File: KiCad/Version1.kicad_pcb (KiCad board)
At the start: 2 copper layers, 41 x 77.7 mm, 82 parts, among them J1 SWD, J2 B4B-XH-A, J3 Conn_01x03_Male, SW1 SW_DPST_x2, SW2 RND 210-00662, SW8 Rotary_Encoder, U1 STM32F411RETx, U2 PMW3389, U3 USBLC6-2P6, U4 AP131-15, U5 AP1117-15, U6 Button, U7 Button, U8 Scroll_button, U9 Button, Y1 16Mhz

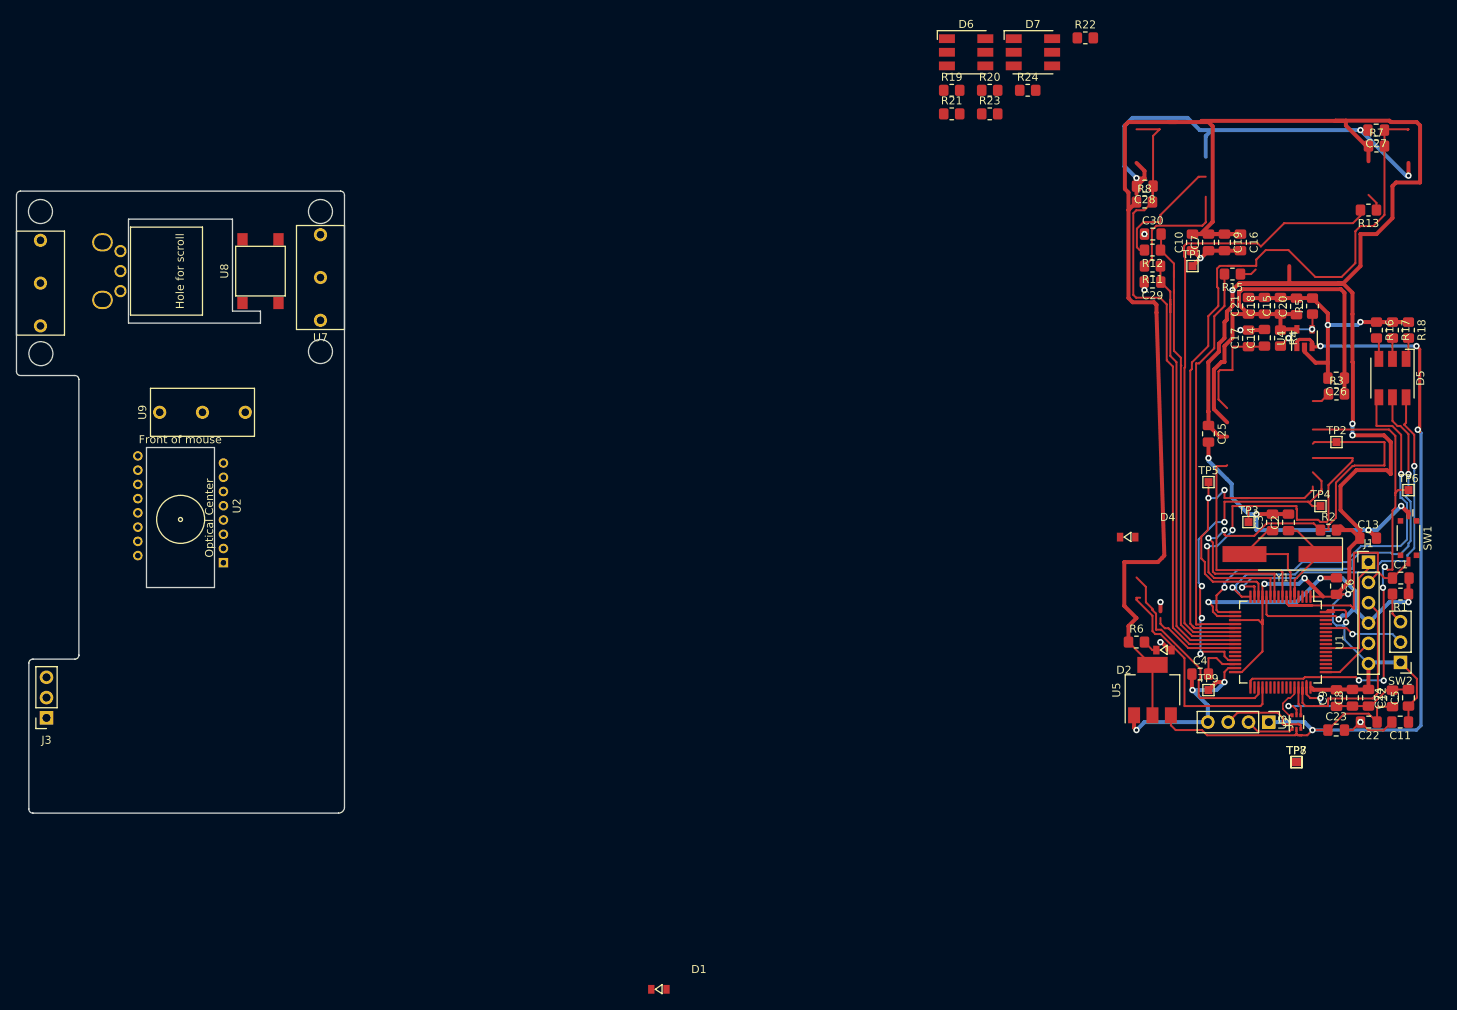
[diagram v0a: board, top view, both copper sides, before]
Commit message: Fixed almost all footprints and nearly the layout of the pcb
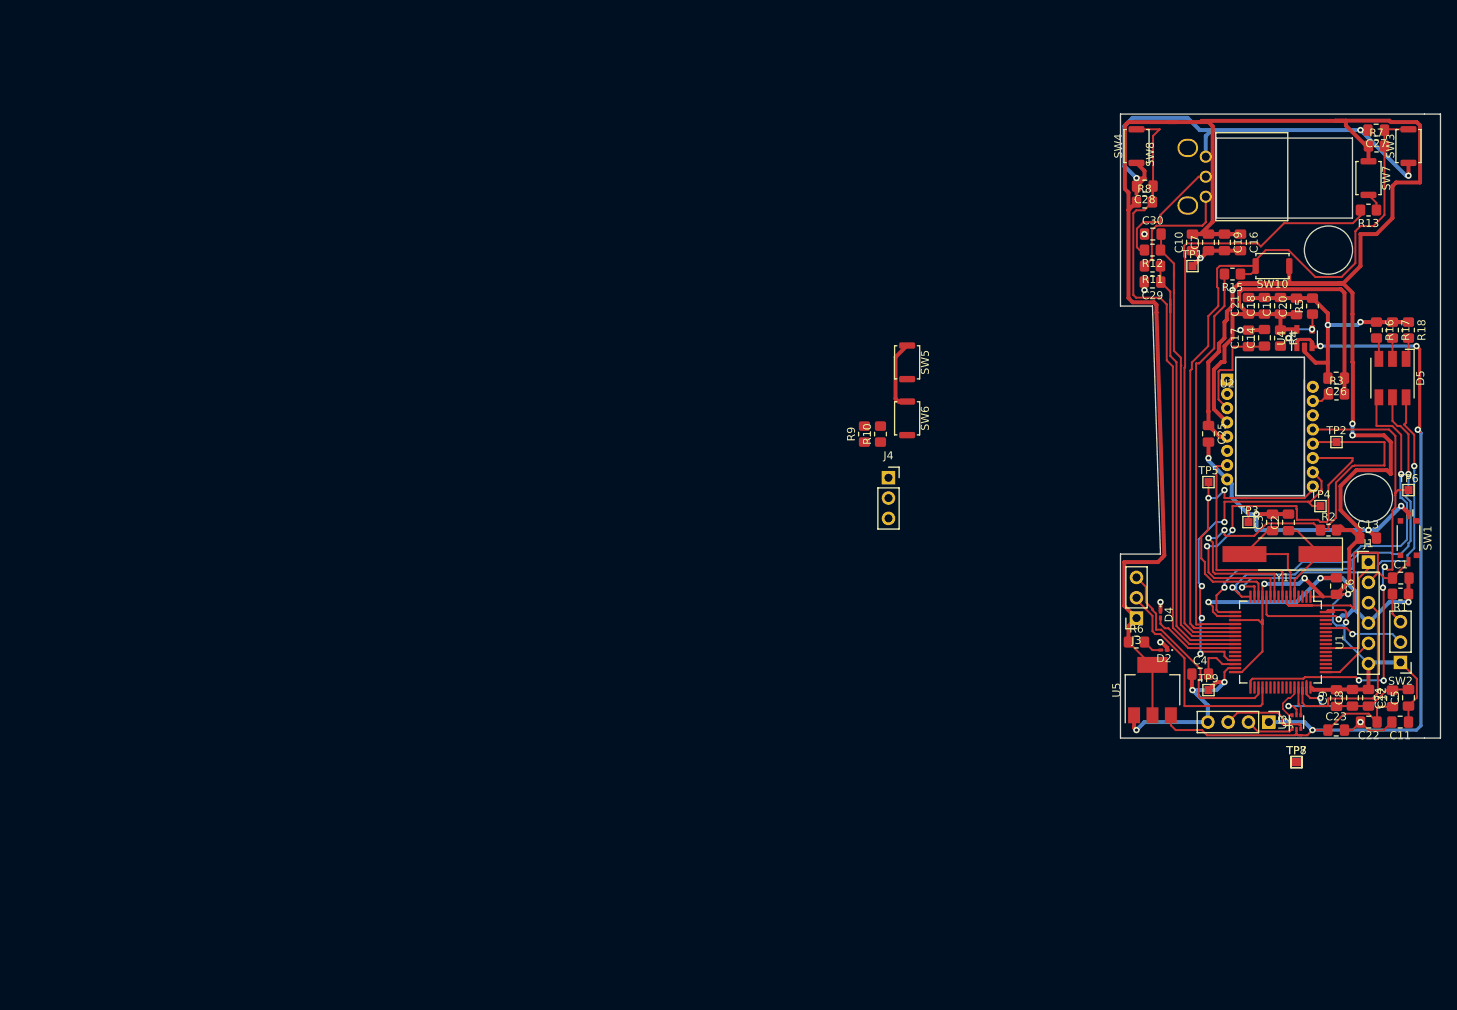
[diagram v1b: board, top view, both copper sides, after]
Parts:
- removed D1: LED, Nuttali:LED
- removed D6, D7: LED_RGB, LED_SMD:LED_RGB_5050-6
- removed R19, R20, R21, R22, R23, R24: 220, Resistor_SMD:R_0805_2012Metric_Pad1.20x1.40mm_HandSolder
- removed U6, U7, U9: Button, Nuttali:D2F-5
- removed U8: Scroll_button, Nuttali:Scroll_button
- added J4: Conn_01x03_Male, Connector_PinSocket_2.54mm:PinSocket_1x03_P2.54mm_Vertical, F.Cu at (161.0, 99.8)
- added R10: 10k, Resistor_SMD:R_0805_2012Metric_Pad1.20x1.40mm_HandSolder, F.Cu at (160.0, 94.3)
- added R9: 10k, Resistor_SMD:R_0805_2012Metric_Pad1.20x1.40mm_HandSolder, F.Cu at (158.0, 94.3)
- added SW10: SW_Push, Button_Switch_SMD:SW_Push_SPST_NO_Alps_SKRK, F.Cu at (209.0, 73.3)
- added SW3: SW_Push, Button_Switch_SMD:SW_Push_SPST_NO_Alps_SKRK, F.Cu at (226.0, 58.3)
- added SW4: SW_Push, Button_Switch_SMD:SW_Push_SPST_NO_Alps_SKRK, F.Cu at (192.0, 58.3)
- added SW5: SW_Push, Button_Switch_SMD:SW_Push_SPST_NO_Alps_SKRK, F.Cu at (163.3, 85.3)
- added SW6: SW_Push, Button_Switch_SMD:SW_Push_SPST_NO_Alps_SKRK, F.Cu at (163.3, 92.3)
- added SW7: SW_Push, Button_Switch_SMD:SW_Push_SPST_NO_Alps_SKRK, F.Cu at (221.0, 62.3)
- D2, D4: footprint Nuttali:LED -> LED_SMD:LED_0201_0603Metric_Pad0.64x0.40mm_HandSolder
- SW8: footprint Nuttali:Encoder -> PMW:Encoder
- U2: footprint Nuttali:PMW3389DM-T3QU -> PMW:PMW3389
- moved J3 136.8 mm to (192.0, 117.3)
- moved SW8 136.2 mm to (198.4, 62.1)
- moved U2 132.0 mm to (203.3, 87.5), turned to 0 degrees
- moved D4 10.5 mm to (195.0, 116.9), turned to 270 degrees
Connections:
- R15 pad 2: VDDIO_3.3V -> Turbo
- R7 pad 1: Net-(R7-Pad1) -> VDDIO_3.3V
- R7 pad 2: VDDIO_3.3V -> RightB
- R8 pad 2: Net-(R8-Pad2) -> LeftB
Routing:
- net VDDIO_3.3V: track 364.3 -> 373.1 mm
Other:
- board size 41 x 77.7 mm -> 40 x 78 mm
